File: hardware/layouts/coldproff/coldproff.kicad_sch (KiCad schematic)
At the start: 13 parts, among them J1 SWD_Header, U1 TPS61221DCKR, U2 STM32L010F4P6, U3 BC65PB-04-STD, U4 TMP117MAIDRCR, U5 ST25DV64KC6

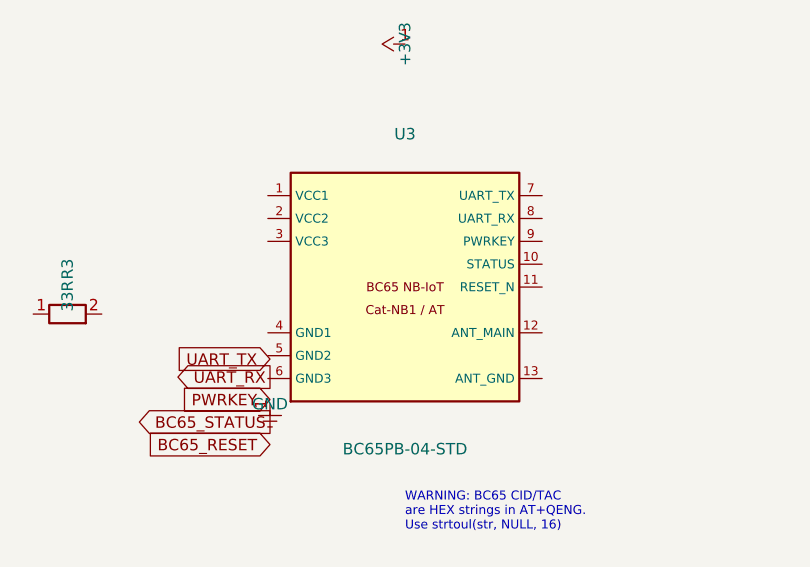
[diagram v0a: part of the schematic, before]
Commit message: Update BC65 schematic symbol, footprint, and PCB for Rev B
- Create Quectel_BC65.pretty/Quectel_BC65.kicad_mod (identical LCC-58
  package to BC66, same pad positions and numbering 1-58)
- Update BC65 lib_symbols: pin numbers now match actual BC65 hardware
  (42/43=VBAT, 1/10/27/36=GND, 7=PWRKEY, 15=RESET_N, 16=NETLIGHT,
  17=MAIN_TXD, 18=MAIN_RXD, 34=GND_ANT, 35=ANT_RF)
- Pin names updated: STATUS→NETLIGHT, UART_TX→MAIN_TXD,
  UART_RX→MAIN_RXD, ANT_MAIN→ANT_RF, VCC1/2→VBAT1/2
- Footprint reference changed from Quectel_BC65:BC65-LCC to
  Quectel_BC65:Quectel_BC65 (in schematic and PCB)
- PCB footprint descriptor updated from BC66 to BC65 with correct
  datasheet URL; 3D model reuses BC66 step (identical physical package)

Co-Authored-By: Claude Sonnet 4.6 <noreply@anthropic.com>
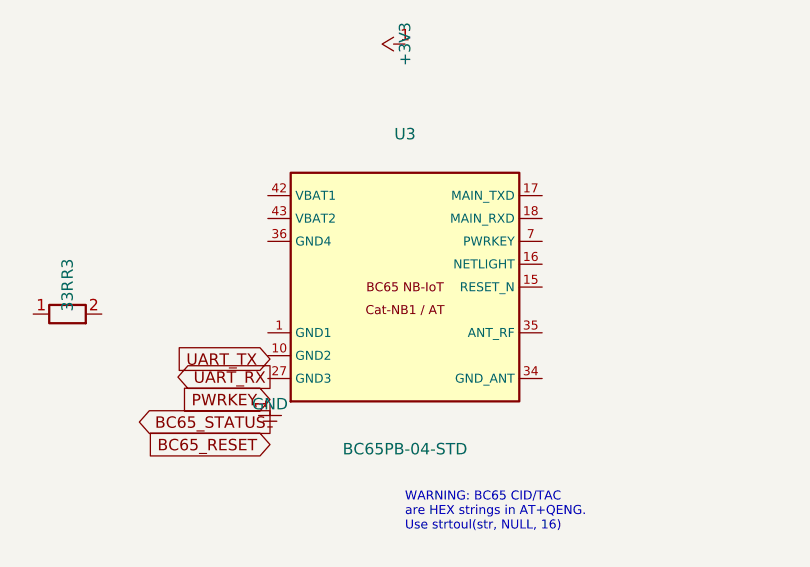
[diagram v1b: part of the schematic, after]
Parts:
- U3: footprint Quectel_BC65:BC65-LCC -> Quectel_BC65:Quectel_BC65
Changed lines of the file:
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@@
 		(property "Reference" "U3" (at 175 128 0) (effects (font (size 1.27 1.27))))
 		(property "Value" "BC65PB-04-STD" (at 175 163 0) (effects (font (size 1.27 1.27))))
-		(property "Footprint" "Quectel_BC65:BC65-LCC" (at 0 0 0) (effects (font (size 1.27 1.27)) (hide yes)))
-		(property "Datasheet" "https://www.quectel.com/product/lpwa-bc65-nb-iot/" (at 0 0 0) (effects (font (size 1.27 1.27)) (hide yes)))
+		(property "Footprint" "Quectel_BC65:Quectel_BC65" (at 0 0 0) (effects (font (size 1.27 1.27)) (hide yes)))
+		(property "Datasheet" "https://www.quectel.com/content/uploads/2024/02/Quectel_BC65_Hardware_Design_V1.0-1.pdf" (at 0 0 0) (effects (font (size 1.27 1.27)) (hide yes)))
+		(pin "42")
+		(pin "43")
+		(pin "36")
 		(pin "1")
-		(pin "2")
-		(pin "3")
-		(pin "4")
-		(pin "5")
-		(pin "6")
+		(pin "10")
+		(pin "27")
+		(pin "17")
+		(pin "18")
 		(pin "7")
-		(pin "8")
-		(pin "9")
-		(pin "10")
-		(pin "11")
-		(pin "12")
-		(pin "13")
+		(pin "16")
+		(pin "15")
+		(pin "35")
+		(pin "34")
 	)
 	(symbol (lib_id "ColdProff:TMP117") (at 280 75 0) (unit 1) (in_bom yes) (on_board yes)

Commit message: Fix missing footprints: B1 battery and C2 tantalum cap
- B1 (LR936): change non-existent BatteryHolder_Keystone_3034_1x9.5mm
  to BatteryHolder_Keystone_2993 (nearest SMT holder in KiCad library)
- C2 (100µF): change CP_EIA-3216-12_HandSoldering to
  CP_EIA-3216-12_Kemet-S_HandSolder (correct library name for same
  EIA-3216 1210 case, hand-solder pads)

Co-Authored-By: Claude Sonnet 4.6 <noreply@anthropic.com>
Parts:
- B1: footprint Battery:BatteryHolder_Keystone_3034_1x9.5mm -> Battery:BatteryHolder_Keystone_2993
- C2: footprint Capacitor_Tantalum_SMD:CP_EIA-3216-12_HandSoldering -> Capacitor_Tantalum_SMD:CP_EIA-3216-12_Kemet-S_HandSolder
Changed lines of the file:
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@@
 		(property "Reference" "B1" (at 33 45 0) (effects (font (size 1.27 1.27))))
 		(property "Value" "LR936" (at 33 48 0) (effects (font (size 1.27 1.27))))
-		(property "Footprint" "Battery:BatteryHolder_Keystone_3034_1x9.5mm" (at 0 0 0) (effects (font (size 1.27 1.27)) (hide yes)))
+		(property "Footprint" "Battery:BatteryHolder_Keystone_2993" (at 0 0 0) (effects (font (size 1.27 1.27)) (hide yes)))
 		(property "Datasheet" "~" (at 0 0 0) (effects (font (size 1.27 1.27)) (hide yes)))
 		(pin "1")
@@
 		(property "Reference" "C2" (at 88 55 0) (effects (font (size 1.27 1.27))))
 		(property "Value" "100uF" (at 88 58 0) (effects (font (size 1.27 1.27))))
-		(property "Footprint" "Capacitor_Tantalum_SMD:CP_EIA-3216-12_HandSoldering" (at 0 0 0) (effects (font (size 1.27 1.27)) (hide yes)))
+		(property "Footprint" "Capacitor_Tantalum_SMD:CP_EIA-3216-12_Kemet-S_HandSolder" (at 0 0 0) (effects (font (size 1.27 1.27)) (hide yes)))
 		(property "Datasheet" "~" (at 0 0 0) (effects (font (size 1.27 1.27)) (hide yes)))
 		(pin "1")

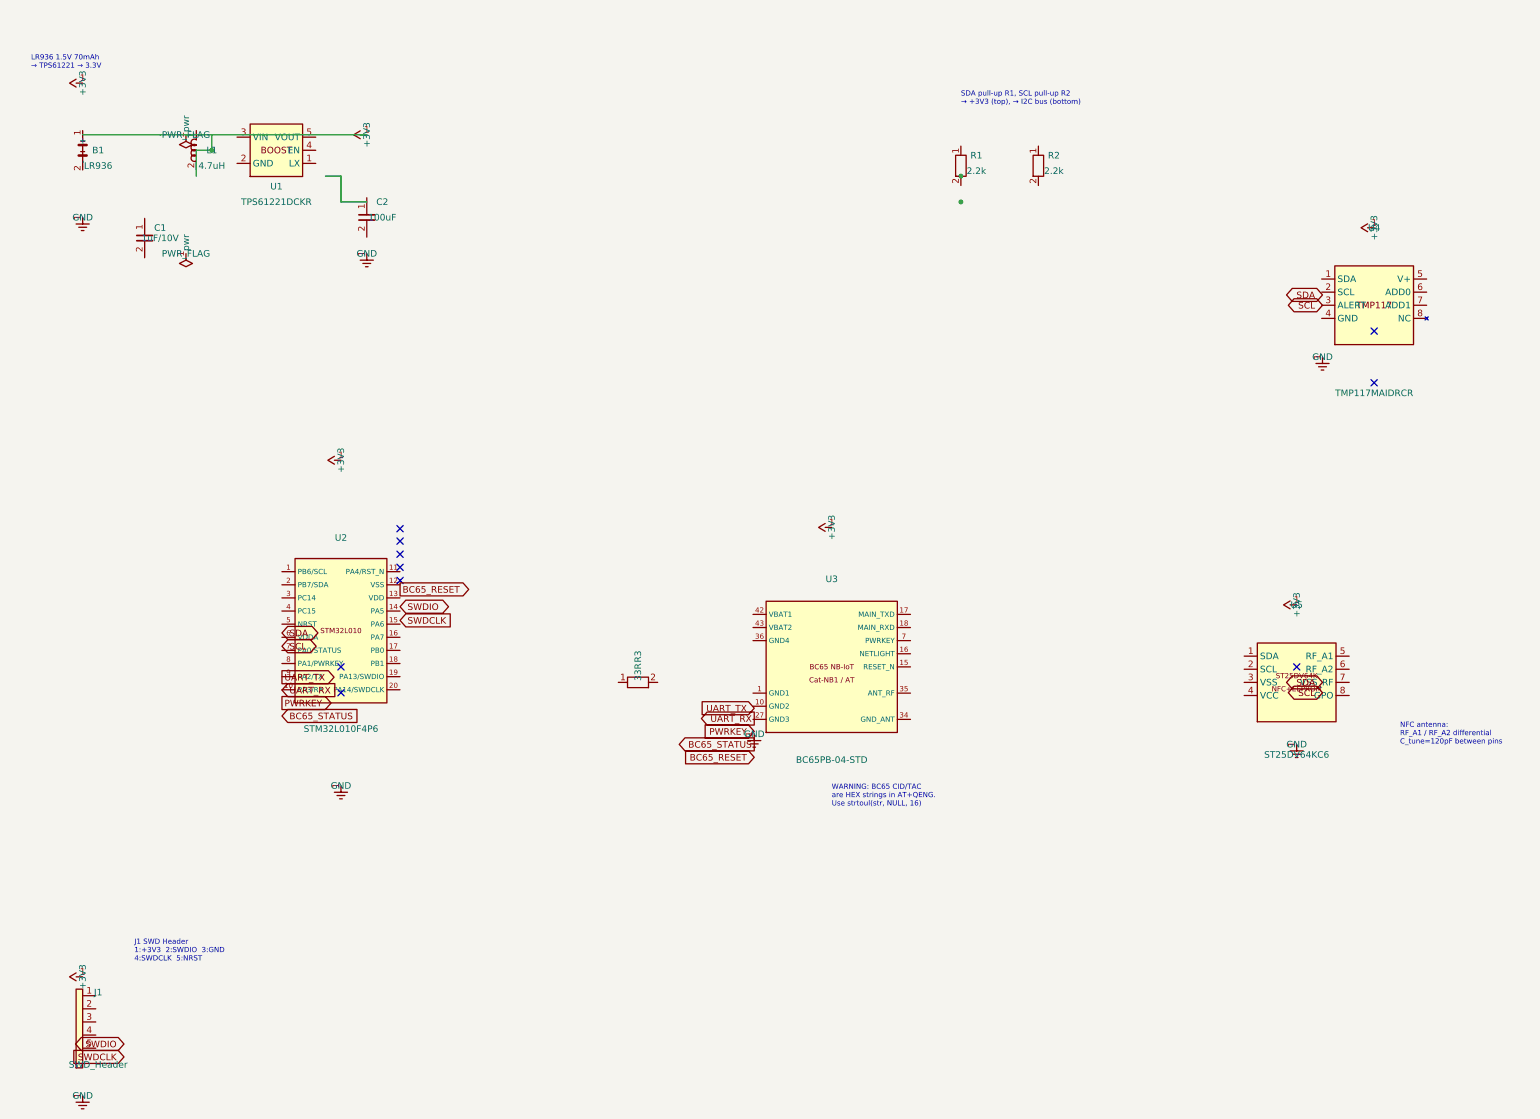
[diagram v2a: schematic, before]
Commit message: Fix schematic readability: power layout, text overlaps, ERC warnings
- Reorganize power circuit (B1, L1, U1, C1, C2) onto 1.27mm grid,
  removing endpoint_off_grid ERC warnings for those components
- Fix all 30 power symbol Value text positions (were overlapping pins)
- Hide redundant stacked power labels in crowded clusters
- Adjust text justification and R3 label positions to clear overlaps
- Add sym-lib-table for PWR/Device/Connector_Generic libraries
  (fixes lib_symbol_issues ERC warnings)
- Add fp-lib-table for local Quectel_BC65 footprint library
- Add KiCad .history/ and lock files to .gitignore

Co-Authored-By: Claude Sonnet 4.6 <noreply@anthropic.com>
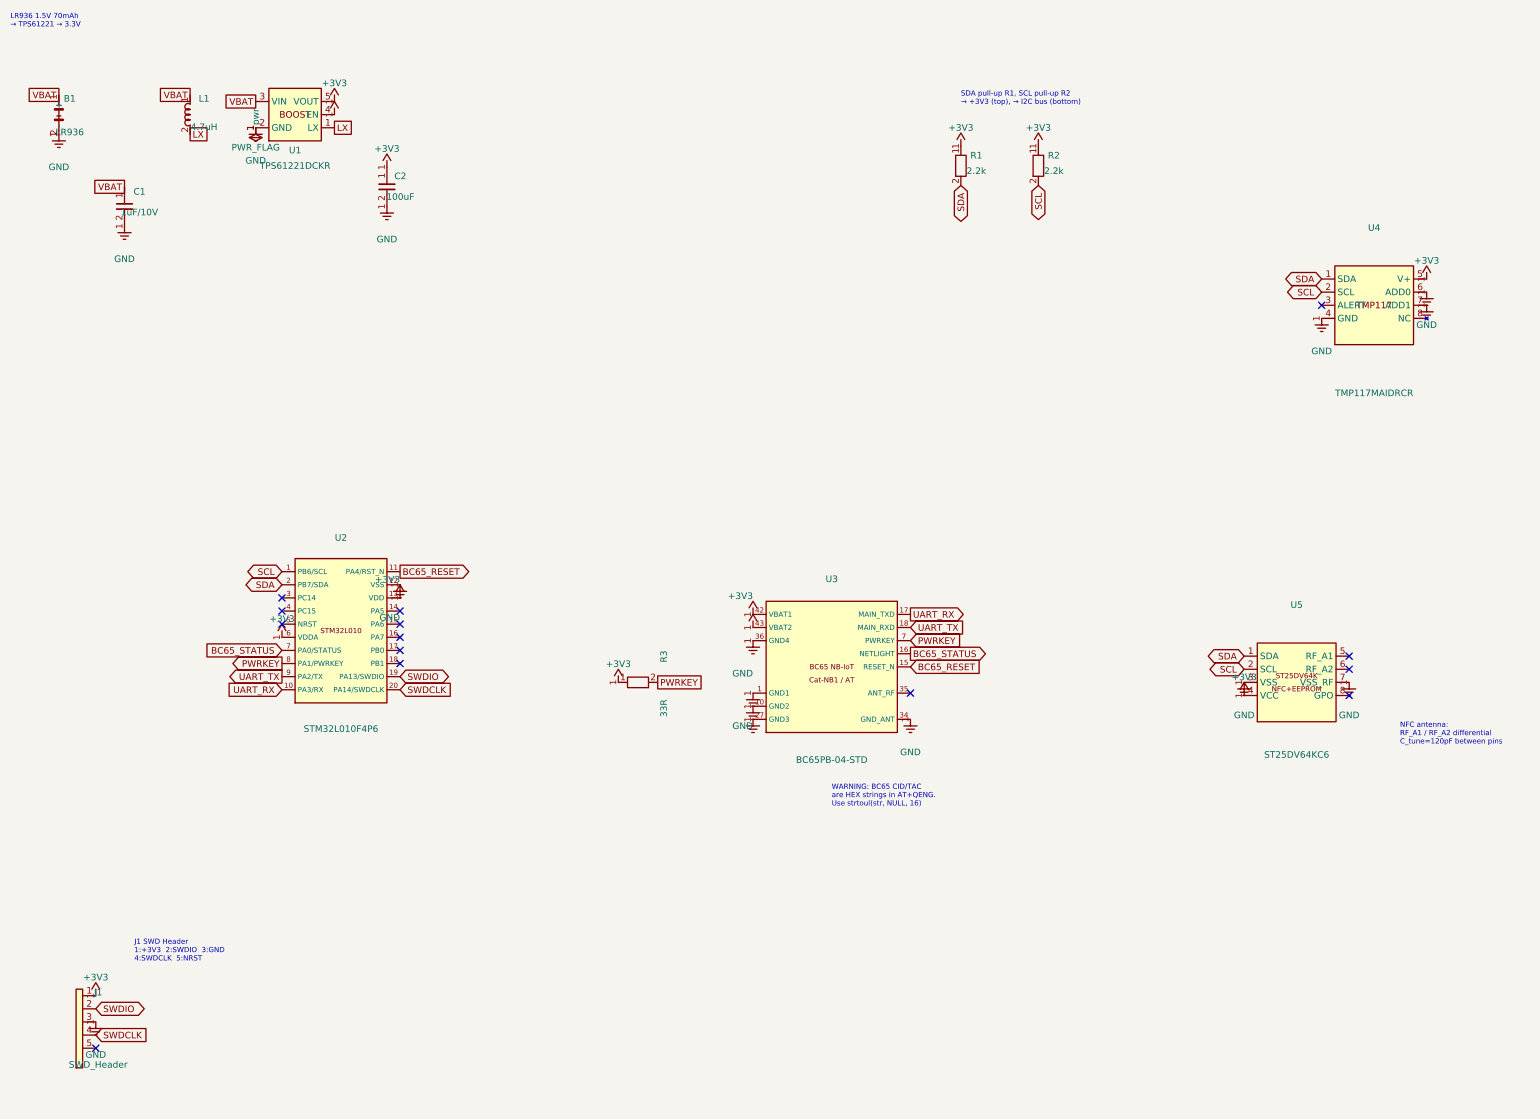
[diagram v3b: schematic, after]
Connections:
- net +3V3: now also C2.1, J1.1 (Pin_1), R1.1, R2.1, R3.1, U1.4 (EN), U1.5 (VOUT), U2.13 (VDD), U2.6 (VDDA), U3.42 (VBAT1), U3.43 (VBAT2), U4.5 (V+), U5.4 (VCC)
- net BC65_RESET: now also U2.11 (PA4/RST_N), U3.15 (RESET_N)
- net BC65_STATUS: now also U2.7 (PA0/STATUS), U3.16 (NETLIGHT)
- net GND: now also B1.2 (-), C1.2, C2.2, J1.3 (Pin_3), U1.2 (GND), U2.12 (VSS), U3.1 (GND1), U3.10 (GND2), U3.27 (GND3), U3.34 (GND_ANT), U3.36 (GND4), U4.4 (GND), U4.6 (ADD0), U4.7 (ADD1), U5.3 (VSS), U5.7 (VSS_RF)
- net PWRKEY: now also R3.2, U2.8 (PA1/PWRKEY), U3.7 (PWRKEY)
- net SCL: now also R2.2, U2.1 (PB6/SCL), U4.2 (SCL), U5.2 (SCL)
- net SDA: now also R1.2, U2.2 (PB7/SDA), U4.1 (SDA), U5.1 (SDA)
- net SWDCLK: now also J1.4 (Pin_4), U2.20 (PA14/SWDCLK)
- net SWDIO: now also J1.2 (Pin_2), U2.19 (PA13/SWDIO)
- net UART_RX: now also U2.10 (PA3/RX), U3.17 (MAIN_TXD)
- net UART_TX: now also U2.9 (PA2/TX), U3.18 (MAIN_RXD)
- net VBAT: now reaches B1.1 (+)
- net VBAT: now also C1.1, L1.1, U1.3 (VIN)
- net LX: now reaches U1.1 (LX)
- net LX: now also L1.2
- no-connect marks 10 -> 14
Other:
- moved on the sheet: B1, C1, C2, L1, U1
